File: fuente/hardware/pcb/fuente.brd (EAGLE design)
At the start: 165.1 x 109.2 mm, 57 parts, among them J1 SEC 18V, J2 SALIDA, J3 TP, Q1 TIP32C, Q2 BC557, Q3 TIP31C, Q4 BC547, U1 LM317T, U2 LM337T, U3 LM317T

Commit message: Fuente: C1 y C2 de 6800 uF/50 V (D28 mm, paso 10 mm) y F2 lento T1A
- Huella de C1/C2 ampliada a 28 mm de diámetro y taladro de 1.3 mm;
  se regeneran .brd/.sch, cobre espejado 1:1 y ensamble (sin cambios de ruteo).
- Cálculos, simulación, esquemáticos, informe, lista de materiales y
  tabla de mediciones actualizados (rizado del filtro 0.73/0.59 V pp).
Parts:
- C1, C2: value 3300u/50V -> 6800u/50V
- F2: value 1A 5x20 -> T1A 5x20
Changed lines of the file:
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@@
 <elements>
 <element name="J1" library="fuente16" package="TERM2" value="SEC 18V" x="7.62" y="50.8" rot="R90"/>
-<element name="F2" library="fuente16" package="FUSE" value="1A 5x20" x="12.7" y="58.42"/>
+<element name="F2" library="fuente16" package="FUSE" value="T1A 5x20" x="12.7" y="58.42"/>
 <element name="D1" library="fuente16" package="DO41" value="1N4007" x="40.64" y="63.5" rot="R90"/>
 <element name="D2" library="fuente16" package="DO41" value="1N4007" x="40.64" y="40.64" rot="R90"/>
-<element name="C1" library="fuente16" package="CPOL25" value="3300u/50V" x="15.24" y="83.82"/>
-<element name="C2" library="fuente16" package="CPOL25" value="3300u/50V" x="15.24" y="25.4"/>
+<element name="C1" library="fuente16" package="CPOL25" value="6800u/50V" x="15.24" y="83.82"/>
+<element name="C2" library="fuente16" package="CPOL25" value="6800u/50V" x="15.24" y="25.4"/>
 <element name="RSC1" library="fuente16" package="RES1W" value="1R8 1W" x="40.64" y="88.9"/>
 <element name="RSC2" library="fuente16" package="RES1W" value="2R2 1W" x="50.8" y="27.94" rot="R270"/>

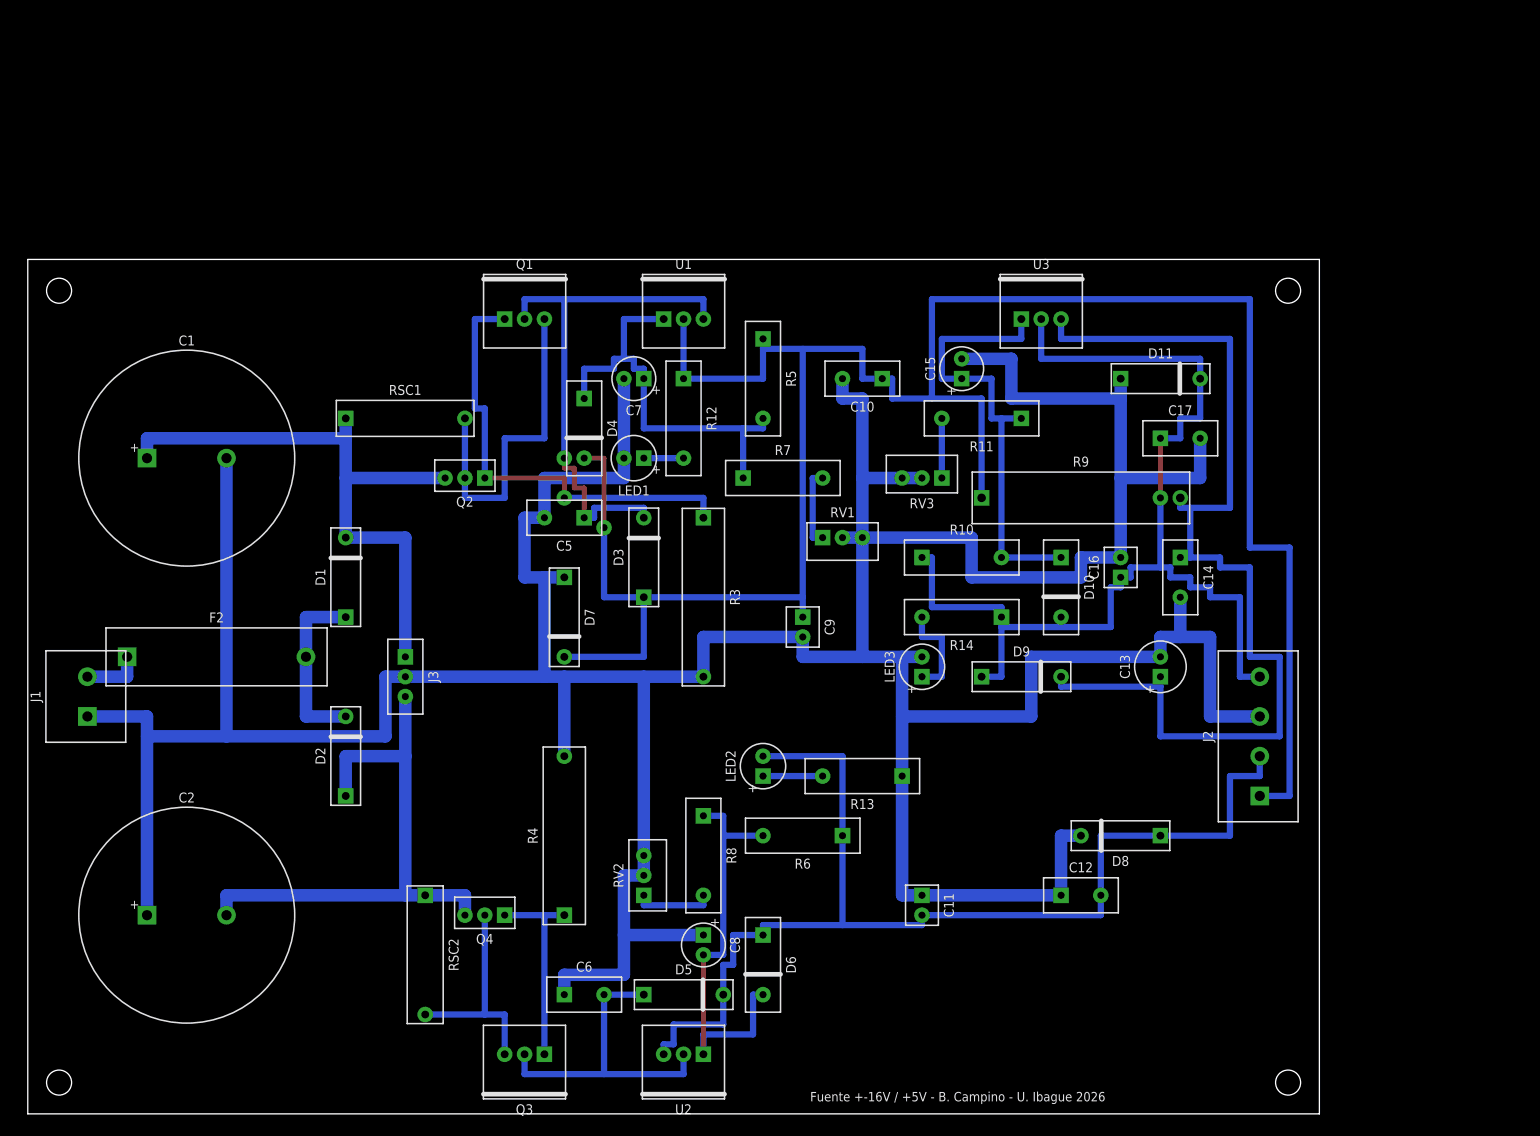
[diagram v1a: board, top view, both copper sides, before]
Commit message: Fuente v2: ±16 V a 1,5 A con ampliación de corriente y foldback
- Transformador 18-0-18 V / 3 A con puente (onda completa); C1 15000 µF y 2x6800 µF reutilizados
- Limitador con foldback (Darlington TIP42C/BD140, sensor BC557) antes de cada regulador
- Ampliación de corriente (Fig. 3-21) con los mismos LM317/LM337
- Carga de prueba RL removible en J4/J5
- Cálculos, simulación (curva V-I, arranque con RL), esquemáticos, placa 190,5 x 139,7 mm,
  lista de materiales, plan de pruebas e informe actualizados
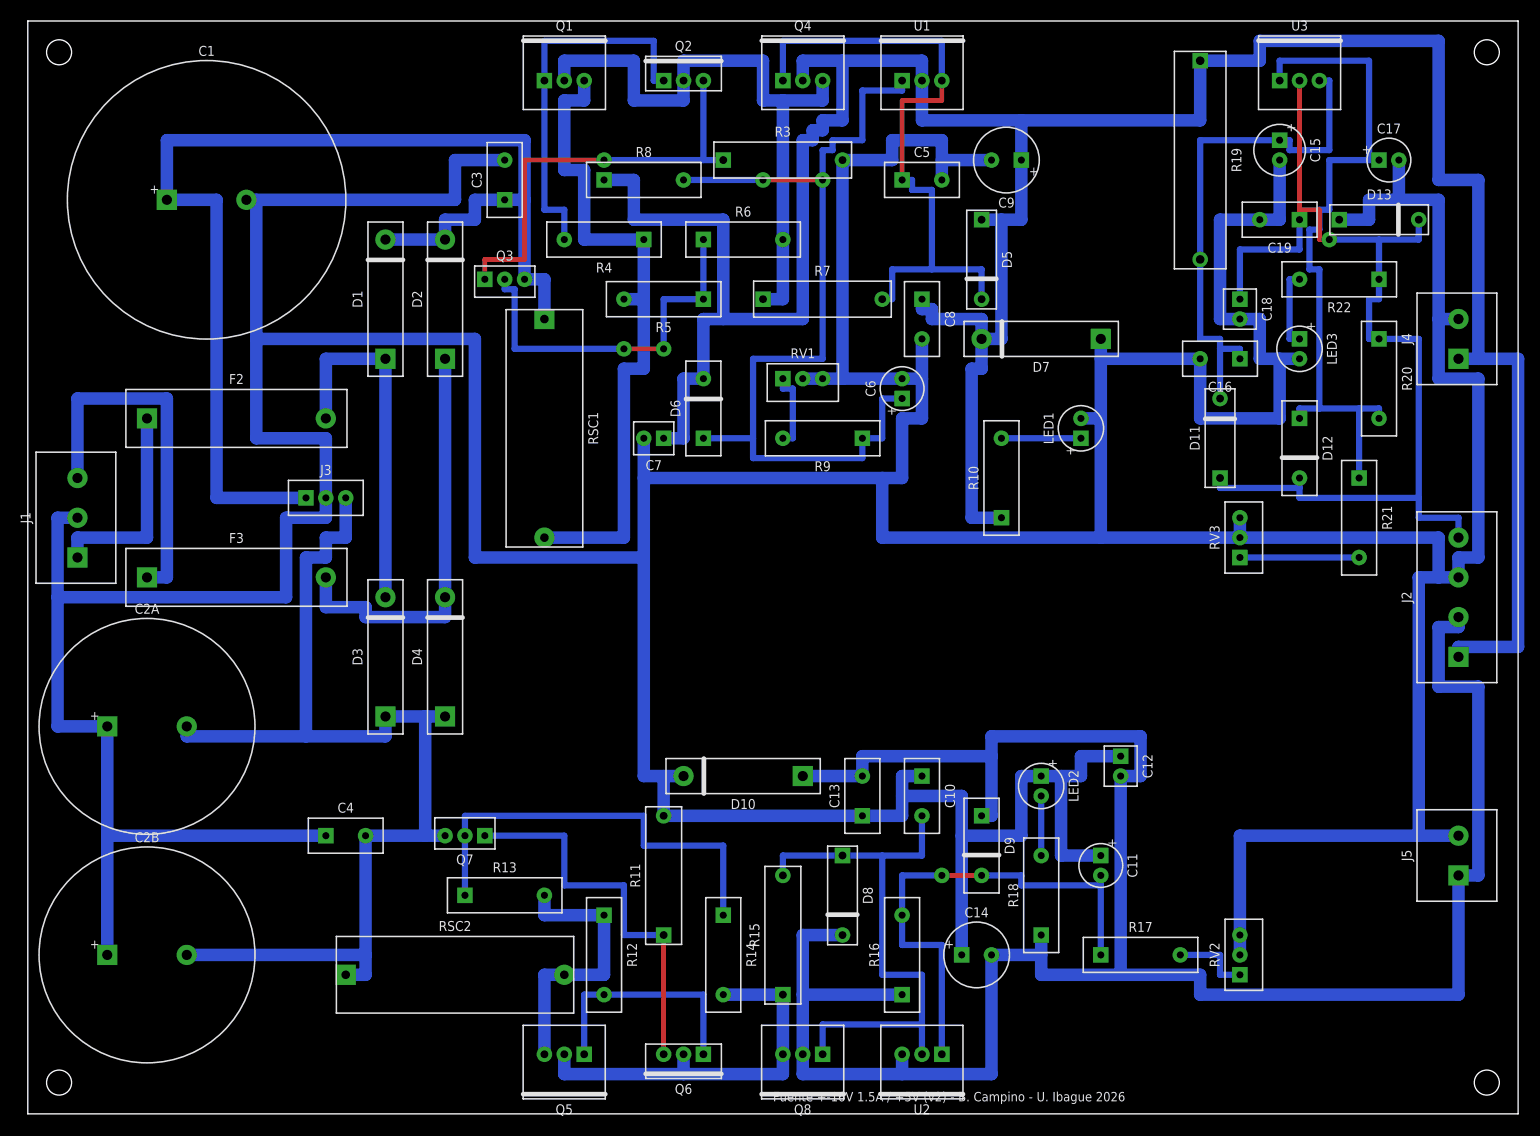
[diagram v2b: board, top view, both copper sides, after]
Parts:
- removed C2: 6800u/50V, fuente16:CPOL25
- added C18: 10u tant, fuente16:CTANT
- added C19, C3, C4: 100n, fuente16:CAP
- added C2A, C2B: 6800u/50V, fuente16:CPOL25
- added D12: 1N4148, fuente16:DO35
- added D13: 1N4007, fuente16:DO41
- added F3: T3.15A, fuente16:FUSE
- added J4: RL +16, fuente16:TERM2
- added J5: RL -16, fuente16:TERM2
- added Q5, Q8: TIP41C, fuente16:TO220
- added Q6: BD139, fuente16:TO126
- added Q7: BC547, fuente16:TO92
- added R15: 2R7 1W, fuente16:RES1W
- added R16, R20: 120 1%, fuente16:RES10
- added R17: 1k3 1%, fuente16:RES10
- added R18: 2k2, fuente16:RES10
- added R19: 100 3W, fuente16:RES3W
- added R21: 330 1%, fuente16:RES10
- added R22: 470, fuente16:RES10
- C1: value 6800u/50V -> 15000u/50V; device fuente16:CPOL25 -> fuente16:CPOL35
- C11: value 10u tant -> 10u/25V; device fuente16:CTANT -> fuente16:CPOL5
- C12: value 100n -> 10u tant; device fuente16:CAP -> fuente16:CTANT
- C13: value 100u/25V -> 100n; device fuente16:CPOL6 -> fuente16:CAP
- C14: value 100n -> 220u/25V; device fuente16:CAP -> fuente16:CPOL8
- C15: value 10u/25V -> 100u/25V; device fuente16:CPOL5 -> fuente16:CPOL6
- C16: value 10u tant -> 100n; device fuente16:CTANT -> fuente16:CAP
- C17, C6: value 100n -> 10u/25V; device fuente16:CAP -> fuente16:CPOL5
- C7: value 10u/25V -> 10u tant; device fuente16:CPOL5 -> fuente16:CTANT
- C8: value 10u/25V -> 100n; device fuente16:CPOL5 -> fuente16:CAP
- C9: value 10u tant -> 220u/25V; device fuente16:CTANT -> fuente16:CPOL8
- D1, D2, D3, D7: value 1N4007 -> 1N5408; device fuente16:DO41 -> fuente16:DIODE
- D10, D4: value 1N4148 -> 1N5408; device fuente16:DO35 -> fuente16:DIODE
- D9: value 1N4007 -> 1N4148; device fuente16:DO41 -> fuente16:DO35
- F2: value T1A 5x20 -> T3.15A
- J1: value SEC 18V -> SEC 18-0-18; device fuente16:TERM2 -> fuente16:TERM3
- Q1: value TIP32C -> TIP42C
- Q2: value BC557 -> BD140; device fuente16:TO92 -> fuente16:TO126
- Q3: value TIP31C -> BC557; device fuente16:TO220 -> fuente16:TO92
- Q4: value BC547 -> TIP42C; device fuente16:TO92 -> fuente16:TO220
- R10: value 120 1% -> 2k2
- R11: value 330 1% -> 2k7 1W; device fuente16:RES10 -> fuente16:RES1W
- R12: value 2k2 -> 1k
- R13: value 2k2 -> 270
- R14: value 470 -> 12k
- R3: value 820 2W -> 2k7 1W; device fuente16:RES2W -> fuente16:RES1W
- R4: value 820 2W -> 1k; device fuente16:RES2W -> fuente16:RES10
- R5: value 120 1% -> 270
- R6: value 120 1% -> 12k
- R7: value 1k3 1% -> 2R7 1W; device fuente16:RES10 -> fuente16:RES1W
- R8: value 1k3 1% -> 120 1%
- R9: value 100 3W -> 1k3 1%; device fuente16:RES3W -> fuente16:RES10
- RSC1: value 1R8 1W -> 0R27 5W; device fuente16:RES1W -> fuente16:RES5W
- RSC2: value 2R2 1W -> 0R27 5W; device fuente16:RES1W -> fuente16:RES5W
- moved Q4 112.5 mm to (96.5, 132.1), turned to 0 degrees
- moved D5 108.1 mm to (121.9, 114.3), turned to 270 degrees
- moved Q3 99.4 mm to (58.4, 106.7), turned to 0 degrees
- moved C6 87.6 mm to (111.8, 91.4), turned to 90 degrees
- moved R4 87.0 mm to (78.7, 111.8), turned to 180 degrees
- moved C8 85.9 mm to (114.3, 104.1)
- moved R8 82.3 mm to (73.7, 119.4), turned to 0 degrees
- moved R11 80.3 mm to (81.3, 22.9), turned to 90 degrees
- moved R6 78.2 mm to (86.4, 111.8), turned to 0 degrees
- moved RV2 76.9 mm to (154.9, 17.8)
- moved D7 75.0 mm to (137.2, 99.1), turned to 180 degrees
- moved R12 69.3 mm to (73.7, 25.4)
- moved C9 64.8 mm to (127.0, 121.9), turned to 180 degrees
- moved LED3 64.8 mm to (162.6, 99.1), turned to 270 degrees
- moved D6 64.0 mm to (86.4, 86.4), turned to 90 degrees
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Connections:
- removed net AC: D1.1, D2.2, F2.2
- removed net ACIN: F2.1, J1.2
- removed net LED2A: LED2.1, R13.2
- removed net VB1: Q1.1, Q2.1, R3.1
- removed net VB3: Q3.1, Q4.1, R4.1
- removed net VE1: Q1.3, Q2.2, RSC1.2
- removed net VE3: Q3.3, Q4.2, RSC2.2
- removed net VIN1: C5.1, D3.2, Q1.2, U1.3
- removed net VIN2: C6.2, D5.1, Q3.2, U2.2
- new net AC1: D1.1, D3.2, F2.2
- new net AC2: D2.1, D4.2, F3.2
- new net ACA: F2.1, J1.1
- new net ACB: F3.1, J1.3
- new net B1: Q1.1, Q2.1, R4.2
- new net B2: Q5.1, Q6.1, R12.2
- new net BD1: Q2.3, Q3.1, R3.1
- new net BD2: Q6.3, Q7.1, R11.1
- new net BS1: Q3.2, R5.1, R6.1
- new net BS2: Q7.2, R13.1, R14.1
- new net E1: Q1.3, R4.1, R5.2, RSC1.2
- new net E2: Q5.3, R12.1, R13.2, RSC2.2
- new net IN1: C5.1, D5.2, Q4.1, R7.2, U1.3
- new net IN2: C10.2, D8.1, Q8.1, R15.2, U2.2
- new net LED2K: LED2.2, R18.2
- new net VA1: Q1.2, Q2.2, Q4.3, R6.2, R7.1
- new net VA2: Q5.2, Q6.2, Q8.3, R14.2, R15.1
- net +16V: now also C7.1, C8.1, D5.1, D6.2, J4.1, Q4.2, R10.1, R19.1, R8.1; no longer C10.1, D3.1, D4.2, R12.1, R5.1, R9.1
- net +5V: now also C18.1, C19.1, D11.1, D12.2, D13.2, R20.1, R22.1; no longer C16.1, C17.1, D10.2, D11.2, D9.1, R10.1, R14.1
- net -16V: now also C13.2, C14.2, D10.1, D8.2, D9.1, J5.1, Q8.2, R16.1, R18.1; no longer C11.2, D5.2, D6.1, D8.1, LED2.2, R6.1
- net ADJ1: now also C6.1, D6.1, R8.2, R9.1; no longer C7.1, D4.1, R5.2, R7.1
- net ADJ2: now also C11.2, D9.2, R16.2, R17.1; no longer C8.2, D6.2, R6.2, R8.1
- net ADJ3: now also C17.1, D12.1, R20.2, R21.1; no longer C15.1, D10.1, R10.2, R11.1
- net GND: now also C10.1, C13.1, C14.1, C18.2, C19.2, C2A.1, C2B.1, C3.2, C4.1, C6.2, C8.2, D10.2, D13.1, J1.2, J4.2, J5.2, LED2.1, R11.2; no longer C10.2, C13.2, C14.2, C2.1, C6.1, C8.1, D11.1, D8.2, J1.1, R13.1, R4.2
- net LED1A: now also R10.2; no longer R12.2
- net LED3A: now also R22.2; no longer R14.2
- net RV1A: now also R9.2; no longer R7.2
- net RV2A: now also R17.2; no longer R8.2
- net RV3A: now also R21.2; no longer R11.2
- net VIN3: now also C15.1, C16.1, D11.2, R19.2; no longer C13.1, C14.1, D9.2, R9.2
- net VRAWN: now also C2A.2, C2B.2, C4.2, D3.1, D4.1, Q7.3; no longer C2.2, D2.1, Q4.3
- net VRAWP: now also C3.1, D2.2, Q3.3; no longer Q2.3
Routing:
- net GND: track 594.4 -> 946.1 mm
- net -16V: track 146.0 -> 293.4 mm
- net +16V: track 293.4 -> 381.0 mm, vias 1 -> 0
- net E1: track 0.00 -> 86.4 mm
- net IN1: track 0.00 -> 83.8 mm
- net VA1: track 0.00 -> 81.3 mm
- net VRAWP: track 78.7 -> 157.5 mm
- net IN2: track 0.00 -> 72.4 mm
- net VIN1: track 68.6 -> 0.00 mm, vias 1 -> 0
- net VRAWN: track 73.7 -> 141.0 mm
- net VIN3: track 132.1 -> 67.3 mm
- net ADJ1: track 54.6 -> 118.1 mm, vias 0 -> 2
- net VB1: track 58.4 -> 0.00 mm, vias 1 -> 0
- net BS2: track 0.00 -> 55.9 mm
- net BD1: track 0.00 -> 55.9 mm, vias 0 -> 1
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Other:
- board size 165.1 x 109.2 mm -> 190.5 x 139.7 mm
- board text added: "Fuente +-16V 1.5A / +5V (v2) - B. Campino - U. Ibague 2026"
- board text removed: "Fuente +-16V / +5V - B. Campino - U. Ibague 2026"
